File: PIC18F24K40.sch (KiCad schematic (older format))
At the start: 4 parts, among them J3 ICSP, U2 PIC18F24K40-I_ML

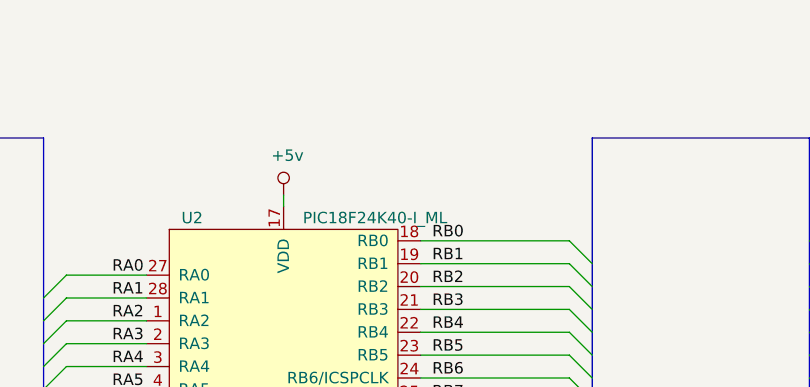
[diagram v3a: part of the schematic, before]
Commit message: Basic layout and schematic capture
SCH:
- added decoupling cap for micro

PCB:
- fill on top layer removed
- decoupling cap placed next to micro

MODEL:
- 1x13 header model flipped to represent the down facing orientation
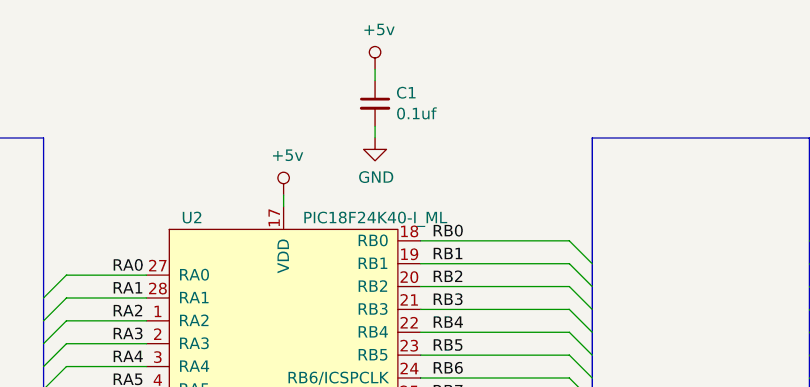
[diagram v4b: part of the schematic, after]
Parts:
- added C1: 0.1uf, _PIC18F24K40:C_0603_1608Metric_Pad1.05x0.95mm_HandSolder, symbol _PIC18F24K40:C_Small
- gave numbers to parts that had none: 2
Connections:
- wire segments 61 -> 63
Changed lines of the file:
@@
 RE3
 $Comp
-L _PIC18F24K40:Conn_01x13 J?
+L _PIC18F24K40:Conn_01x13 J1
 U 1 1 5BD10226
 P 1450 4300
-F 0 "J?" H 1370 5117 50  0000 C CNN
+F 0 "J1" H 1370 5117 50  0000 C CNN
 F 1 "Conn_01x13" H 1370 5026 50  0000 C CNN
 F 2 "_PIC18F24K40:PinHeader_1x13_P2.54mm_Vertical" H 1450 4300 50  0001 C CNN
@@
 $EndComp
 $Comp
-L _PIC18F24K40:Conn_01x13 J?
+L _PIC18F24K40:Conn_01x13 J2
 U 1 1 5BD14518
 P 6900 4400
-F 0 "J?" H 6980 4442 50  0000 L CNN
+F 0 "J2" H 6980 4442 50  0000 L CNN
 F 1 "Conn_01x13" H 6980 4351 50  0000 L CNN
 F 2 "_PIC18F24K40:PinHeader_1x13_P2.54mm_Vertical" H 6900 4400 50  0001 C CNN
@@
 $EndComp
 $Comp
-L _PIC18F24K40:+5v #PWR?
+L _PIC18F24K40:+5v #PWR0101
 U 1 1 5BD1682D
 P 6550 3800
-F 0 "#PWR?" H 6550 3650 50  0001 C CNN
+F 0 "#PWR0101" H 6550 3650 50  0001 C CNN
 F 1 "+5v" V 6567 3973 50  0000 C CNN
 F 2 "" H 6550 3800 50  0001 C CNN
@@
 $EndComp
 $Comp
-L _PIC18F24K40:GND #PWR?
+L _PIC18F24K40:GND #PWR0102
 U 1 1 5BD1690C
 P 6550 3900
-F 0 "#PWR?" H 6550 3650 50  0001 C CNN
+F 0 "#PWR0102" H 6550 3650 50  0001 C CNN
 F 1 "GND" V 6555 3727 50  0000 C CNN
 F 2 "" H 6550 3900 50  0001 C CNN
@@
 	6700 3900 6550 3900
 $Comp
-L _PIC18F24K40:+5v #PWR?
+L _PIC18F24K40:+5v #PWR0103
 U 1 1 5BD1A8A9
 P 3950 3700
-F 0 "#PWR?" H 3950 3550 50  0001 C CNN
+F 0 "#PWR0103" H 3950 3550 50  0001 C CNN
 F 1 "+5v" H 3967 3873 50  0000 C CNN
 F 2 "" H 3950 3700 50  0001 C CNN
@@
 $EndComp
 $Comp
-L _PIC18F24K40:GND #PWR?
+L _PIC18F24K40:GND #PWR0104
 U 1 1 5BD1A8CD
 P 3900 5650
-F 0 "#PWR?" H 3900 5400 50  0001 C CNN
+F 0 "#PWR0104" H 3900 5400 50  0001 C CNN
 F 1 "GND" H 3905 5477 50  0000 C CNN
 F 2 "" H 3900 5650 50  0001 C CNN
@@
 Wire Wire Line
 	3950 3750 3950 3700
+$Comp
+L _PIC18F24K40:C_Small C1
+U 1 1 5BD236CD
+P 4350 3300
+F 0 "C1" H 4442 3346 50  0000 L CNN
+F 1 "0.1uf" H 4442 3255 50  0000 L CNN
+F 2 "_PIC18F24K40:C_0603_1608Metric_Pad1.05x0.95mm_HandSolder" H 4350 3300 50  0001 C CNN
+F 3 "~" H 4350 3300 50  0001 C CNN
+	1    4350 3300
+	1    0    0    -1
+$EndComp
+$Comp
+L _PIC18F24K40:GND #PWR02
+U 1 1 5BD23938
+P 4350 3450
+F 0 "#PWR02" H 4350 3200 50  0001 C CNN
+F 1 "GND" H 4355 3277 50  0000 C CNN
+F 2 "" H 4350 3450 50  0001 C CNN
+F 3 "" H 4350 3450 50  0001 C CNN
+	1    4350 3450
+	1    0    0    -1
+$EndComp
+$Comp
+L _PIC18F24K40:+5v #PWR01
+U 1 1 5BD2394D
+P 4350 3150
+F 0 "#PWR01" H 4350 3000 50  0001 C CNN
+F 1 "+5v" H 4367 3323 50  0000 C CNN
+F 2 "" H 4350 3150 50  0001 C CNN
+F 3 "" H 4350 3150 50  0001 C CNN
+	1    4350 3150
+	1    0    0    -1
+$EndComp
+Wire Wire Line
+	4350 3150 4350 3200
+Wire Wire Line
+	4350 3400 4350 3450
 Wire Bus Line
 	5300 5100 5300 6050

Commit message: USB and FTDI circuit added
I've added a datasheet for usb micro connector I plan on using.

SCH:
- USB and FTDI placed with supporting passives

PCB:
- Initial layout of USB micro and FTDI chip done
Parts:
- added C2, C3: 47pf, _PIC18F24K40:C_0603_1608Metric_Pad1.05x0.95mm_HandSolder, symbol _PIC18F24K40:C_Small
- added C4, C5: 0.1uf, _PIC18F24K40:C_0603_1608Metric_Pad1.05x0.95mm_HandSolder, symbol _PIC18F24K40:C_Small
- added FB1: TBD, _PIC18F24K40:C_0603_1608Metric_Pad1.05x0.95mm_HandSolder, symbol _PIC18F24K40:Ferrite_Bead_Small
- added J4: USB_B_Micro, _PIC18F24K40:USB_Micro-B_Molex_47346-0001, symbol _PIC18F24K40:USB_B_Micro
- added R1, R2: 27, _PIC18F24K40:R_0603_1608Metric_Pad1.05x0.95mm_HandSolder, symbol _PIC18F24K40:R_Small_US
- added R3: 10k, _PIC18F24K40:R_0603_1608Metric_Pad1.05x0.95mm_HandSolder, symbol _PIC18F24K40:R_Small_US
- added U1: FT231XQ, _PIC18F24K40:QFN-20-1EP_4x4mm_P0.5mm_EP2.5x2.5mm, symbol _PIC18F24K40:FT231XQ
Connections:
- net labels added: +5v_USB
- net labels removed: +5v
- wire segments 63 -> 101
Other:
- note added: "PIC18F24K40"
- note added: "PICKIT programmer headder"
- note added: "RX1"
- note added: "TX1"

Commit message: Initial route complete
This may be the design I get prototyped, unless I can think of anything
I would like to change in the next few days.

Outputs updated so the files can be viewed without kicad. Fab outputs
will be generated and commited when I get the prototypes fabbed.
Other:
- moved on the sheet: C1
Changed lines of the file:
@@
 L _PIC18F24K40:C_Small C1
 U 1 1 5BD236CD
-P 4350 3300
-F 0 "C1" H 4442 3346 50  0000 L CNN
-F 1 "0.1uf" H 4442 3255 50  0000 L CNN
-F 2 "_PIC18F24K40:C_0603_1608Metric_Pad1.05x0.95mm_HandSolder" H 4350 3300 50  0001 C CNN
-F 3 "~" H 4350 3300 50  0001 C CNN
-	1    4350 3300
+P 5600 4500
+F 0 "C1" H 5692 4546 50  0000 L CNN
+F 1 "0.1uf" H 5692 4455 50  0000 L CNN
+F 2 "_PIC18F24K40:C_0603_1608Metric_Pad1.05x0.95mm_HandSolder" H 5600 4500 50  0001 C CNN
+F 3 "~" H 5600 4500 50  0001 C CNN
+	1    5600 4500
 	1    0    0    -1
 $EndComp
@@
 L _PIC18F24K40:GND #PWR02
 U 1 1 5BD23938
-P 4350 3450
-F 0 "#PWR02" H 4350 3200 50  0001 C CNN
-F 1 "GND" H 4355 3277 50  0000 C CNN
-F 2 "" H 4350 3450 50  0001 C CNN
-F 3 "" H 4350 3450 50  0001 C CNN
-	1    4350 3450
-	1    0    0    -1
-$EndComp
-Wire Wire Line
-	4350 3400 4350 3450
+P 5600 4650
+F 0 "#PWR02" H 5600 4400 50  0001 C CNN
+F 1 "GND" H 5605 4477 50  0000 C CNN
+F 2 "" H 5600 4650 50  0001 C CNN
+F 3 "" H 5600 4650 50  0001 C CNN
+	1    5600 4650
+	1    0    0    -1
+$EndComp
+Wire Wire Line
+	5600 4600 5600 4650
 $Comp
 L _PIC18F24K40:FT231XQ U1
@@
 L _PIC18F24K40:+5v_USB #PWR0111
 U 1 1 5BDE87E9
-P 4350 3150
-F 0 "#PWR0111" H 4350 3000 50  0001 C CNN
-F 1 "+5v_USB" H 4367 3323 50  0000 C CNN
-F 2 "" H 4350 3150 50  0001 C CNN
-F 3 "" H 4350 3150 50  0001 C CNN
-	1    4350 3150
-	1    0    0    -1
-$EndComp
-Wire Wire Line
-	4350 3150 4350 3200
+P 5600 4350
+F 0 "#PWR0111" H 5600 4200 50  0001 C CNN
+F 1 "+5v_USB" H 5617 4523 50  0000 C CNN
+F 2 "" H 5600 4350 50  0001 C CNN
+F 3 "" H 5600 4350 50  0001 C CNN
+	1    5600 4350
+	1    0    0    -1
+$EndComp
+Wire Wire Line
+	5600 4350 5600 4400
 Wire Bus Line
 	5300 5100 5300 6050

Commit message: Ordering information added to schematic elements
Manufacturer and part number added.
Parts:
- FB1: value TBD -> 330 Ohms @ 100MHz; Manufacturer (none) -> Murata Electronics North America; Manufacturer Part Number (none) -> BLM18SG331TN1D
- J1, J2: Manufacturer (none) -> Sullins Connector Solutions; Manufacturer Part Number (none) -> PREC013SAAN-RC
- J3: Manufacturer (none) -> Sullins Connector Solutions; Manufacturer Part Number (none) -> PREC006SABN-RC
- J4: Manufacturer (none) -> Molex, LLC; Manufacturer Part Number (none) -> 0473460001
- U1: Manufacturer (none) -> FTDI, Future Technology Devices International Ltd; Manufacturer Part Number (none) -> FT231XQ-R
- U2: Manufacturer (none) -> Microchip Technology; Manufacturer Part Number (none) -> PIC18F24K40T-I/ML
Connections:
- wire segments 101 -> 105
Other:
- moved on the sheet: C1, C2, C3, C4, C5, J3, U2

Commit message: Option for using sockets
Part numbers and models for female connections added
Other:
- note added: "Alternate part number for female header:\nPPTC131LFBN-RC"
- note added: "Alternate part number for right angle\nPRPC006SBAN-M71RC"
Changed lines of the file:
@@
 Wire Bus Line
 	3400 4100 3400 5650
+Text Notes 7900 4550 0    50   ~ 0
+Alternate part number for female header:\nPPTC131LFBN-RC
+Text Notes 8100 3150 0    50   ~ 0
+Alternate part number for right angle\nPRPC006SBAN-M71RC
 $EndSCHEMATC
